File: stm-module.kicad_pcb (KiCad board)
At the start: 2 copper layers, 4 parts, among them U1 STM32G474RETx, U2 TPS7A20xxxDBV

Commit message: add crystal
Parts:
- added C10: 15pF, Capacitor_THT:C_Disc_D5.0mm_W2.5mm_P5.00mm, F.Cu at (136.5, 85.5)
- added C11: 15pF, Capacitor_THT:C_Disc_D5.0mm_W2.5mm_P5.00mm, F.Cu at (136.5, 89.6)
- added C3: 100nF, Capacitor_SMD:C_0805_2012Metric, F.Cu at (122.7, 105.5)
- added C4: 100nF, Capacitor_SMD:C_0805_2012Metric, F.Cu at (127.2, 99.5)
- added C5: 100nF, Capacitor_SMD:C_0805_2012Metric, F.Cu at (127.2, 102.5)
- added C6: 100nF, Capacitor_SMD:C_0805_2012Metric, F.Cu at (127.2, 105.5)
- added C7: 100nF, Capacitor_SMD:C_0805_2012Metric, F.Cu at (131.6, 99.5)
- added C8: 100nF, Capacitor_SMD:C_0805_2012Metric, F.Cu at (131.6, 102.5)
- added C9: 1uF, Capacitor_SMD:C_0805_2012Metric, F.Cu at (131.6, 105.5)
- added R1: 10kΩ, Resistor_SMD:R_0805_2012Metric, F.Cu at (145.2, 93.1)
- added R2: 10kΩ, Resistor_SMD:R_0805_2012Metric, F.Cu at (145.2, 96.0)
- added SW1: Reset, Button_Switch_THT:SW_PUSH_6mm, F.Cu at (135.9, 100.0)
- added Y1: Crystal, Crystal:Crystal_SMD_0603-2Pin_6.0x3.5mm, F.Cu at (139.0, 94.4)
- C1, C2: value 1uf -> 1uF
- moved U2 47.0 mm to (136.4, 108.9)
- moved U1 45.5 mm to (127.7, 90.7)
- moved C2 40.7 mm to (122.7, 102.5)
- moved C1 40.7 mm to (122.7, 99.5)
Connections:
- U1 pad 1: unconnected-(U1-VBAT-Pad1) -> /3.3V
- U1 pad 15: Net-(U1-VSS-Pad15) -> /GND
- U1 pad 27: unconnected-(U1-VSSA-Pad27) -> /GND
- U1 pad 28: unconnected-(U1-VREF+-Pad28) -> /3.3V
- U1 pad 31: Net-(U1-VSS-Pad15) -> /GND
- U1 pad 47: Net-(U1-VSS-Pad15) -> /GND
- U1 pad 5: unconnected-(U1-PF0-Pad5) -> Net-(U1-PF0)
- U1 pad 6: unconnected-(U1-PF1-Pad6) -> Net-(U1-PF1)
- U1 pad 61: unconnected-(U1-PB8-Pad61) -> Net-(U1-PB8)
- U1 pad 63: Net-(U1-VSS-Pad15) -> /GND
- U1 pad 7: unconnected-(U1-PG10-Pad7) -> Net-(U1-PG10)

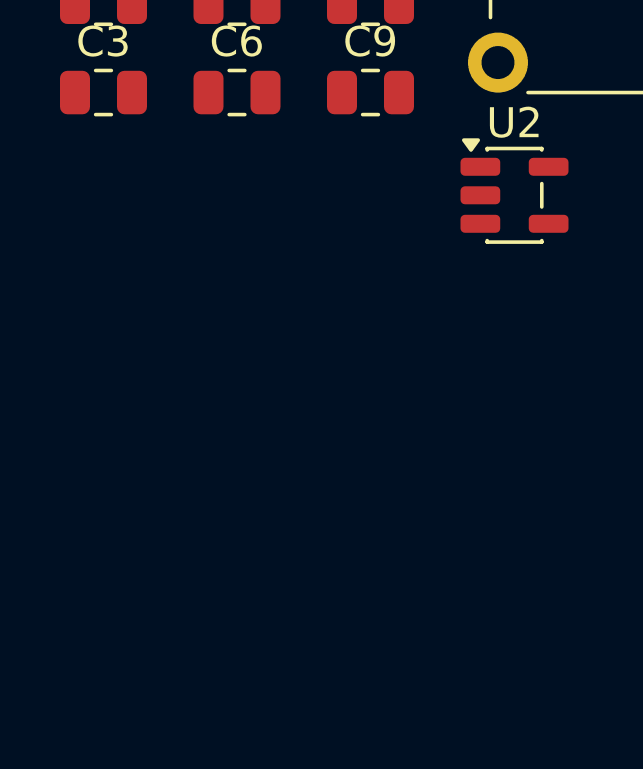
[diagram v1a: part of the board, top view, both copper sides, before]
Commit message: add more caps
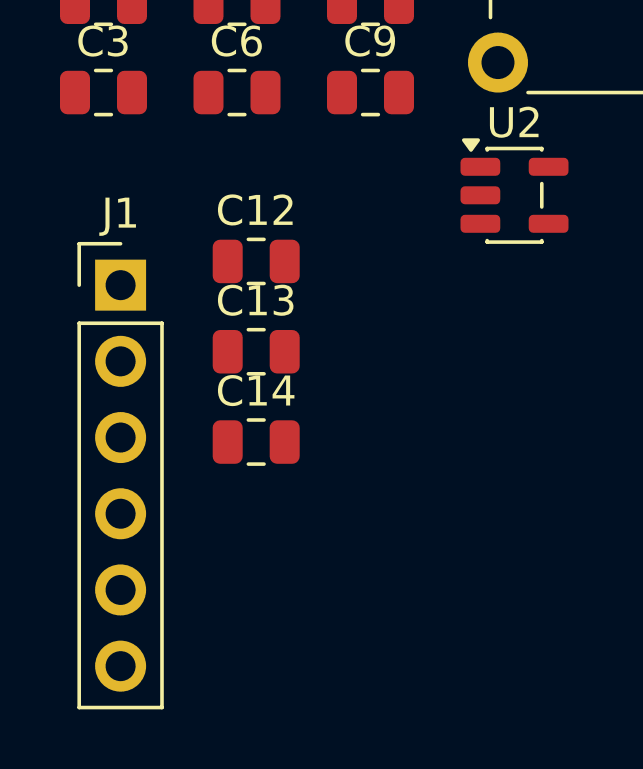
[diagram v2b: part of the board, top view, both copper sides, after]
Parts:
- added C12: 4.7uF, Capacitor_SMD:C_0805_2012Metric, F.Cu at (127.8, 111.1)
- added C13: 100nF, Capacitor_SMD:C_0805_2012Metric, F.Cu at (127.8, 114.1)
- added C14: 1uF, Capacitor_SMD:C_0805_2012Metric, F.Cu at (127.8, 117.1)
- added J1: SWD, Connector_PinHeader_2.54mm:PinHeader_1x06_P2.54mm_Vertical, F.Cu at (123.3, 111.9)
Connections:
- net Net-(U1-PG10) renamed /NRST
- U1 pad 49: unconnected-(U1-PA13-Pad49) -> Net-(J1-Pin_3)
- U1 pad 50: unconnected-(U1-PA14-Pad50) -> Net-(J1-Pin_4)
- U1 pad 56: unconnected-(U1-PB3-Pad56) -> Net-(J1-Pin_6)

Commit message: pcb work
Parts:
- added J2: connectorL, Connector_PinHeader_2.54mm:PinHeader_2x20_P2.54mm_Vertical, B.Cu at (140.5, 85.3)
- added J3: connectorR, Connector_PinHeader_2.54mm:PinHeader_2x20_P2.54mm_Vertical, B.Cu at (185.0, 83.7)
- moved J1 59.1 mm to (166.3, 71.3), turned to -90 degrees
- moved C1 50.6 mm to (169.1, 119.8)
- moved C9 48.5 mm to (177.9, 119.8)
- moved C5 41.8 mm to (168.3, 109.9), turned to -135 degrees
- moved C6 36.7 mm to (163.5, 100.0), turned to -45 degrees
- moved C12 36.7 mm to (163.6, 119.3)
- moved C14 36.7 mm to (163.6, 125.3)
- moved C3 36.1 mm to (154.7, 122.3)
- moved U1 36.1 mm to (159.7, 107.5), turned to 45 degrees
- moved C2 36.1 mm to (154.7, 119.3)
- moved C7 35.8 mm to (159.2, 122.3)
- moved C8 35.8 mm to (159.2, 125.3)
- moved U2 35.5 mm to (165.6, 129.2)
- moved C4 34.4 mm to (157.3, 116.1), turned to 135 degrees
- moved SW1 34.3 mm to (154.5, 128.8)
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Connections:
- net /3.3V renamed +3.3V
- net /5V renamed +5V
- net /GND renamed GND
- net Net-(J1-Pin_3) renamed /PA13
- net Net-(J1-Pin_4) renamed /PA14
- net Net-(J1-Pin_6) renamed /PB3
- net Net-(U1-PB8) renamed /PB8
- U1 pad 10: unconnected-(U1-PC2-Pad10) -> /PC2
- U1 pad 11: unconnected-(U1-PC3-Pad11) -> /PC3
- U1 pad 12: unconnected-(U1-PA0-Pad12) -> /PA0
- U1 pad 13: unconnected-(U1-PA1-Pad13) -> /PA1
- U1 pad 14: unconnected-(U1-PA2-Pad14) -> /PA2
- U1 pad 17: unconnected-(U1-PA3-Pad17) -> /PA3
- U1 pad 18: unconnected-(U1-PA4-Pad18) -> /PA4
- U1 pad 19: unconnected-(U1-PA5-Pad19) -> /PA5
- U1 pad 2: unconnected-(U1-PC13-Pad2) -> /PC13
- U1 pad 20: unconnected-(U1-PA6-Pad20) -> /PA6
- U1 pad 21: unconnected-(U1-PA7-Pad21) -> /PA7
- U1 pad 22: unconnected-(U1-PC4-Pad22) -> /PC4
- U1 pad 23: unconnected-(U1-PC5-Pad23) -> /PC5
- U1 pad 24: unconnected-(U1-PB0-Pad24) -> /PB0
- U1 pad 25: unconnected-(U1-PB1-Pad25) -> /PB1
- U1 pad 26: unconnected-(U1-PB2-Pad26) -> /PB2
- U1 pad 3: unconnected-(U1-PC14-Pad3) -> /PC14
- U1 pad 30: unconnected-(U1-PB10-Pad30) -> /PB10
- U1 pad 33: unconnected-(U1-PB11-Pad33) -> /PB11
- U1 pad 34: unconnected-(U1-PB12-Pad34) -> /PB12
- U1 pad 35: unconnected-(U1-PB13-Pad35) -> /PB13
- U1 pad 36: unconnected-(U1-PB14-Pad36) -> /PB14
- U1 pad 37: unconnected-(U1-PB15-Pad37) -> /PB15
- U1 pad 38: unconnected-(U1-PC6-Pad38) -> /PC6
- U1 pad 39: unconnected-(U1-PC7-Pad39) -> /PC7
- U1 pad 4: unconnected-(U1-PC15-Pad4) -> /PC15
- U1 pad 40: unconnected-(U1-PC8-Pad40) -> /PC8
- U1 pad 41: unconnected-(U1-PC9-Pad41) -> /PC9
- U1 pad 42: unconnected-(U1-PA8-Pad42) -> /PA8
- U1 pad 43: unconnected-(U1-PA9-Pad43) -> /PA9
- U1 pad 44: unconnected-(U1-PA10-Pad44) -> /PA10
- U1 pad 45: unconnected-(U1-PA11-Pad45) -> /PA11
- U1 pad 46: unconnected-(U1-PA12-Pad46) -> /PA12
- U1 pad 51: unconnected-(U1-PA15-Pad51) -> /PA15
- U1 pad 52: unconnected-(U1-PC10-Pad52) -> /PC10
- U1 pad 53: unconnected-(U1-PC11-Pad53) -> /PC11
- U1 pad 54: unconnected-(U1-PC12-Pad54) -> /PC12
- U1 pad 55: unconnected-(U1-PD2-Pad55) -> /PD2
- U1 pad 57: unconnected-(U1-PB4-Pad57) -> /PB4
- U1 pad 58: unconnected-(U1-PB5-Pad58) -> /PB5
- U1 pad 59: unconnected-(U1-PB6-Pad59) -> /PB6
- U1 pad 60: unconnected-(U1-PB7-Pad60) -> /PB7
- U1 pad 62: unconnected-(U1-PB9-Pad62) -> /PB9
- U1 pad 8: unconnected-(U1-PC0-Pad8) -> /PC0
- U1 pad 9: unconnected-(U1-PC1-Pad9) -> /PC1
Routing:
- net +3.3V: track 0.00 -> 7.98 mm
- added copper zone on F.Cu, net GND
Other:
- board outline added: 86.3 x 83.5 mm

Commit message: updates
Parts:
- moved SW1 57.6 mm to (182.2, 78.2)
- moved C3 33.0 mm to (186.2, 132.0), turned to -135 degrees
- moved C7 32.7 mm to (173.4, 92.8), turned to 45 degrees
- moved C2 31.7 mm to (176.2, 142.5), turned to 90 degrees
- moved Y1 29.2 mm to (169.9, 139.2)
- moved C4 27.8 mm to (176.2, 136.5)
- moved J2 27.4 mm to (162.4, 101.8)
- moved C10 27.1 mm to (171.0, 79.9)
- moved C8 25.7 mm to (184.4, 130.1), turned to -45 degrees
- moved C14 25.4 mm to (187.7, 133.4), turned to -135 degrees
- moved U1 25.0 mm to (176.4, 126.0)
- moved C13 22.9 mm to (167.2, 125.8)
- moved C5 22.9 mm to (185.4, 125.1), turned to 45 degrees
- moved C11 22.4 mm to (179.9, 96.1)
- moved U2 21.4 mm to (180.1, 144.9)
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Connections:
- J3 pad 1: unconnected-(J3-Pin_1-Pad1) -> GND
- J3 pad 10: unconnected-(J3-Pin_10-Pad10) -> /PC7
- J3 pad 11: unconnected-(J3-Pin_11-Pad11) -> /PB14
- J3 pad 12: unconnected-(J3-Pin_12-Pad12) -> /PB15
- J3 pad 13: unconnected-(J3-Pin_13-Pad13) -> /PB12
- J3 pad 14: unconnected-(J3-Pin_14-Pad14) -> /PB13
- J3 pad 15: unconnected-(J3-Pin_15-Pad15) -> +3.3V
- J3 pad 16: unconnected-(J3-Pin_16-Pad16) -> /PB11
- J3 pad 17: unconnected-(J3-Pin_17-Pad17) -> GND
- J3 pad 18: unconnected-(J3-Pin_18-Pad18) -> GND
- J3 pad 19: unconnected-(J3-Pin_19-Pad19) -> GND
- J3 pad 2: unconnected-(J3-Pin_2-Pad2) -> /PA12
- J3 pad 20: unconnected-(J3-Pin_20-Pad20) -> GND
- J3 pad 21: unconnected-(J3-Pin_21-Pad21) -> GND
- J3 pad 22: unconnected-(J3-Pin_22-Pad22) -> GND
- J3 pad 23: unconnected-(J3-Pin_23-Pad23) -> GND
- J3 pad 24: unconnected-(J3-Pin_24-Pad24) -> GND
- J3 pad 25: unconnected-(J3-Pin_25-Pad25) -> GND
- J3 pad 26: unconnected-(J3-Pin_26-Pad26) -> GND
- J3 pad 27: unconnected-(J3-Pin_27-Pad27) -> GND
- J3 pad 28: unconnected-(J3-Pin_28-Pad28) -> GND
- J3 pad 29: unconnected-(J3-Pin_29-Pad29) -> /PB10
- J3 pad 3: unconnected-(J3-Pin_3-Pad3) -> /PA10
- J3 pad 30: unconnected-(J3-Pin_30-Pad30) -> +3.3V
- J3 pad 31: unconnected-(J3-Pin_31-Pad31) -> /PB2
- J3 pad 32: unconnected-(J3-Pin_32-Pad32) -> /PB1
- J3 pad 33: unconnected-(J3-Pin_33-Pad33) -> /PB0
- J3 pad 34: unconnected-(J3-Pin_34-Pad34) -> /PC5
- J3 pad 35: unconnected-(J3-Pin_35-Pad35) -> /PC4
- J3 pad 36: unconnected-(J3-Pin_36-Pad36) -> /PA7
- J3 pad 37: unconnected-(J3-Pin_37-Pad37) -> /PA6
- J3 pad 38: unconnected-(J3-Pin_38-Pad38) -> /PA5
- J3 pad 39: unconnected-(J3-Pin_39-Pad39) -> /PA4
- J3 pad 4: unconnected-(J3-Pin_4-Pad4) -> /PA11
- J3 pad 40: unconnected-(J3-Pin_40-Pad40) -> /PA3
- J3 pad 5: unconnected-(J3-Pin_5-Pad5) -> /PA8
- J3 pad 6: unconnected-(J3-Pin_6-Pad6) -> /PA9
- J3 pad 7: unconnected-(J3-Pin_7-Pad7) -> /PC8
- J3 pad 8: unconnected-(J3-Pin_8-Pad8) -> /PC9
- J3 pad 9: unconnected-(J3-Pin_9-Pad9) -> /PC6
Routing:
- net GND: track 0.00 -> 44.0 mm
- net /PA4: track 0.00 -> 24.9 mm
- net /PA12: track 0.00 -> 23.2 mm
- net /PA10: track 0.00 -> 23.2 mm
- net /PA6: track 0.00 -> 22.8 mm
- net /PA3: track 0.00 -> 22.6 mm
- net /PA8: track 0.00 -> 21.0 mm
- net /PA11: track 0.00 -> 20.9 mm
- net /PC4: track 0.00 -> 20.6 mm
- net /PA5: track 0.00 -> 20.5 mm
- net /PC8: track 0.00 -> 18.9 mm
- net /PA9: track 0.00 -> 18.7 mm
- net /PB0: track 0.00 -> 18.5 mm
- net /PA7: track 0.00 -> 18.4 mm
- net /PC6: track 0.00 -> 16.8 mm
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- added copper zone on B.Cu, net GND

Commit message: pcb updates
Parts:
- added C15: 10uF, Capacitor_SMD:C_0805_2012Metric, F.Cu at (178.3, 147.8)
- added J4: power, Connector_PinHeader_2.54mm:PinHeader_1x04_P2.54mm_Vertical, F.Cu at (174.1, 150.7)
- C12: value 4.7uF -> 10uF
- C13, C3, C4, C5, C6, C7, C8: footprint Capacitor_SMD:C_0805_2012Metric -> Capacitor_SMD:C_0603_1608Metric
- moved C11 46.2 mm to (165.3, 140.0), turned to 45 degrees
- moved C12 45.8 mm to (186.1, 151.1), turned to 180 degrees
- moved C10 41.1 mm to (164.6, 120.5), turned to -90 degrees
- moved C1 39.6 mm to (185.6, 148.2), turned to -90 degrees
- moved SW1 30.2 mm to (175.4, 107.7), turned to -45 degrees
- moved C7 29.9 mm to (167.9, 122.2), turned to -90 degrees
- moved C3 19.4 mm to (168.0, 125.3), turned to -90 degrees
- moved C13 17.1 mm to (183.6, 130.6)
- moved C6 15.3 mm to (179.4, 117.3), turned to -135 degrees
- moved R1 15.0 mm to (181.7, 114.7), turned to 45 degrees
- moved Y1 8.84 mm to (167.7, 130.6), turned to 135 degrees
- moved C2 3.83 mm to (178.3, 145.7), turned to 180 degrees
- moved U2 3.18 mm to (182.4, 147.1)
- moved C14 2.86 mm to (186.4, 130.9), turned to 135 degrees
- moved C9 2.53 mm to (187.4, 126.6), turned to 45 degrees
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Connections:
- C13 pad 1: +3.3V -> GND
- C13 pad 2: GND -> +3.3V
- C2 pad 2: +5V -> GND
- C4 pad 1: +3.3V -> GND
- C4 pad 2: GND -> +3.3V
- C5 pad 1: +3.3V -> GND
- C5 pad 2: GND -> +3.3V
- C6 pad 1: +3.3V -> GND
- C6 pad 2: GND -> +3.3V
- C7 pad 1: +3.3V -> GND
- C7 pad 2: GND -> +3.3V
- C8 pad 1: +3.3V -> GND
- C8 pad 2: GND -> +3.3V
- J2 pad 10: unconnected-(J2-Pin_10-Pad10) -> /PB4
- J2 pad 11: unconnected-(J2-Pin_11-Pad11) -> /PB5
- J2 pad 12: unconnected-(J2-Pin_12-Pad12) -> /PB6
- J2 pad 13: unconnected-(J2-Pin_13-Pad13) -> /PB7
- J2 pad 14: unconnected-(J2-Pin_14-Pad14) -> /PB8
- J2 pad 15: unconnected-(J2-Pin_15-Pad15) -> /PB9
- J2 pad 16: unconnected-(J2-Pin_16-Pad16) -> +3.3V
- J2 pad 17: unconnected-(J2-Pin_17-Pad17) -> /PC13
- J2 pad 18: unconnected-(J2-Pin_18-Pad18) -> /PC14
- J2 pad 19: unconnected-(J2-Pin_19-Pad19) -> /PC15
- J2 pad 2: unconnected-(J2-Pin_2-Pad2) -> /PA13
- J2 pad 21: unconnected-(J2-Pin_21-Pad21) -> GND
- J2 pad 22: unconnected-(J2-Pin_22-Pad22) -> GND
- J2 pad 23: unconnected-(J2-Pin_23-Pad23) -> GND
- J2 pad 24: unconnected-(J2-Pin_24-Pad24) -> GND
- J2 pad 25: unconnected-(J2-Pin_25-Pad25) -> GND
- J2 pad 26: unconnected-(J2-Pin_26-Pad26) -> GND
- J2 pad 27: unconnected-(J2-Pin_27-Pad27) -> GND
- J2 pad 28: unconnected-(J2-Pin_28-Pad28) -> GND
- J2 pad 29: unconnected-(J2-Pin_29-Pad29) -> GND
- J2 pad 3: unconnected-(J2-Pin_3-Pad3) -> /PA14
- J2 pad 30: unconnected-(J2-Pin_30-Pad30) -> GND
- J2 pad 31: unconnected-(J2-Pin_31-Pad31) -> GND
- J2 pad 32: unconnected-(J2-Pin_32-Pad32) -> GND
- J2 pad 33: unconnected-(J2-Pin_33-Pad33) -> /PC0
- J2 pad 34: unconnected-(J2-Pin_34-Pad34) -> GND
- J2 pad 35: unconnected-(J2-Pin_35-Pad35) -> /PC2
- J2 pad 36: unconnected-(J2-Pin_36-Pad36) -> /PC1
- J2 pad 37: unconnected-(J2-Pin_37-Pad37) -> /PA0
- J2 pad 38: unconnected-(J2-Pin_38-Pad38) -> /PC3
- J2 pad 39: unconnected-(J2-Pin_39-Pad39) -> /PA2
- J2 pad 4: unconnected-(J2-Pin_4-Pad4) -> /PA15
- J2 pad 40: unconnected-(J2-Pin_40-Pad40) -> /PA1
- J2 pad 5: unconnected-(J2-Pin_5-Pad5) -> /PC10
- J2 pad 6: unconnected-(J2-Pin_6-Pad6) -> /PC11
- J2 pad 7: unconnected-(J2-Pin_7-Pad7) -> /PC12
- J2 pad 8: unconnected-(J2-Pin_8-Pad8) -> /PD2
- J2 pad 9: unconnected-(J2-Pin_9-Pad9) -> /PB3
- J3 pad 15: +3.3V -> /PB10
- J3 pad 17: GND -> +3.3V
- J3 pad 29: /PB10 -> GND
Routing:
- net +3.3V: track 21.5 -> 251.1 mm
- net GND: track 44.0 -> 17.0 mm, vias 0 -> 6
- net /PA1: track 0.00 -> 25.3 mm
- net /PA13: track 0.00 -> 25.0 mm
- net /PC3: track 0.00 -> 23.9 mm
- net /PA2: track 0.00 -> 23.1 mm
- net /NRST: track 0.00 -> 23.0 mm
- net /PA15: track 0.00 -> 22.9 mm
- net /PC1: track 0.00 -> 22.5 mm
- net /PA0: track 0.00 -> 21.5 mm
- net /PC11: track 0.00 -> 20.7 mm
- net /PA14: track 0.00 -> 20.6 mm
- net /PC2: track 0.00 -> 20.1 mm
- net /PD2: track 0.00 -> 19.2 mm
- net /PC0: track 0.00 -> 18.8 mm
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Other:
- board size 86.3 x 83.5 mm -> 39.3 x 83.5 mm

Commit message: finish main routing
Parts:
- J1: value SWD -> Conn_01x05_Pin; footprint Connector_PinHeader_2.54mm:PinHeader_1x06_P2.54mm_Vertical -> Connector_PinHeader_2.54mm:PinHeader_1x05_P2.54mm_Vertical
- moved J1 32.5 mm to (170.3, 103.6), turned to 90 degrees
- moved R2 27.3 mm to (165.3, 117.7), turned to -90 degrees
- moved C4 0.10 mm to (175.2, 135.2)
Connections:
- J1 pad 1: +3.3V -> /NRST
- J1 pad 2: GND -> /PA13
- J1 pad 3: /PA13 -> /PA14
- J1 pad 4: /PA14 -> GND
- J1 pad 5: /NRST -> +3.3V
- J3 pad 30: +3.3V -> GND
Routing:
- net /PA14: track 20.6 -> 45.6 mm
- net /PA13: track 25.0 -> 39.7 mm
- net /NRST: track 23.0 -> 37.6 mm
- net GND: track 17.0 -> 21.4 mm
- net +3.3V: track 251.1 -> 248.2 mm
- net /PB7: track 12.7 -> 14.1 mm
- net /PB8: track 15.1 -> 16.4 mm
- net /PB9: track 12.0 -> 12.8 mm
- net /PB6: track 16.4 -> 17.2 mm
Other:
- board size 39.3 x 83.5 mm -> 39.3 x 56.1 mm

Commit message: more pcb updates
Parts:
- added D1: PWR LED, LED_SMD:LED_0805_2012Metric, F.Cu at (176.0, 141.1)
- added D2: RUN LED, LED_SMD:LED_0805_2012Metric, F.Cu at (178.1, 141.1)
- added D3: CAN LED, LED_SMD:LED_0805_2012Metric, F.Cu at (180.2, 141.1)
- added D4: FAULT LED, LED_SMD:LED_0805_2012Metric, F.Cu at (182.3, 141.1)
- added J5: USB_C_Receptacle_USB2.0_16P, Connector_USB:USB_C_Receptacle_HRO_TYPE-C-31-M-12, F.Cu at (182.9, 101.2)
- added R3: 330Ω, Resistor_SMD:R_0805_2012Metric, F.Cu at (173.9, 141.8)
- added R4: 220Ω, Resistor_SMD:R_0805_2012Metric, F.Cu at (178.1, 137.7)
- added R5: 1kΩ, Resistor_SMD:R_0805_2012Metric, F.Cu at (180.2, 137.7)
- added R6: 1kΩ, Resistor_SMD:R_0805_2012Metric, F.Cu at (182.3, 137.7)
- added R7: 5.1kΩ, Resistor_SMD:R_0805_2012Metric, F.Cu at (185.6, 107.4)
- added R8: 5.1kΩ, Resistor_SMD:R_0805_2012Metric, F.Cu at (180.8, 107.4)
- added REF**: MountingHole_3.2mm_M3, MountingHole:MountingHole_3.2mm_M3, F.Cu at (196.8, 99.3)
- added REF**: MountingHole_3.2mm_M3, MountingHole:MountingHole_3.2mm_M3, F.Cu at (196.7, 153.8)
- added REF**: MountingHole_3.2mm_M3, MountingHole:MountingHole_3.2mm_M3, F.Cu at (156.3, 99.2)
- added REF**: MountingHole_3.2mm_M3, MountingHole:MountingHole_3.2mm_M3, F.Cu at (156.2, 153.7)
- moved SW1 7.84 mm to (176.7, 115.5), turned to 135 degrees
- moved J1 5.39 mm to (165.4, 101.3)
- moved R1 0.32 mm to (181.4, 114.6)
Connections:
- J2 pad 20: unconnected-(J2-Pin_20-Pad20) -> GND
- J3 pad 2: /PA12 -> unconnected-(J3-Pin_2-Pad2)
- J3 pad 4: /PA11 -> unconnected-(J3-Pin_4-Pad4)
- U1 pad 45: /PA11 -> /D-
- U1 pad 46: /PA12 -> /D+
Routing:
- net +3.3V: track 248.2 -> 299.9 mm
- net /PA12: track 23.2 -> 0.00 mm
- net /PA11: track 20.9 -> 0.00 mm
- net /D-: track 0.00 -> 20.0 mm
- net /D+: track 0.00 -> 19.6 mm
- net /NRST: track 37.6 -> 46.5 mm
- net Net-(J5-VBUS-PadA4): track 0.00 -> 6.99 mm
- net /PA14: track 45.6 -> 39.7 mm
- net /PA13: track 39.7 -> 34.3 mm
- net Net-(D1-A): track 0.00 -> 2.40 mm
- net Net-(J5-SBU1): track 0.00 -> 2.21 mm
- net Net-(J5-SBU2): track 0.00 -> 2.21 mm
- net /PA3: track 22.6 -> 24.6 mm
- net Net-(D4-A): track 0.00 -> 1.55 mm
- net Net-(D3-A): track 0.00 -> 1.55 mm
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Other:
- board size 39.3 x 56.1 mm -> 45.2 x 59.1 mm

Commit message: final changes
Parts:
- removed the REF** at (196.8, 99.3)
- removed the REF** at (196.7, 153.8)
- removed the REF** at (156.3, 99.2)
- removed the REF** at (156.2, 153.7)
- added REF**: MountingHole_3.2mm_M3, MountingHole:MountingHole_3.2mm_M3, F.Cu at (196.8, 99.3)
- added REF**: MountingHole_3.2mm_M3, MountingHole:MountingHole_3.2mm_M3, F.Cu at (196.9, 153.7)
- added REF**: MountingHole_3.2mm_M3, MountingHole:MountingHole_3.2mm_M3, F.Cu at (156.2, 153.8)
- added REF**: MountingHole_3.2mm_M3, MountingHole:MountingHole_3.2mm_M3, F.Cu at (156.2, 99.3)
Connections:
- J3 pad 17: +3.3V -> GND
- J3 pad 2: unconnected-(J3-Pin_2-Pad2) -> /D+
- J3 pad 4: unconnected-(J3-Pin_4-Pad4) -> /D-
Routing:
- net /D+: track 19.6 -> 27.6 mm
- net /D-: track 20.0 -> 27.3 mm
- net Net-(J5-VBUS-PadA4): track 6.99 -> 0.00 mm
- net +3.3V: track 299.9 -> 299.0 mm
- net /NRST: track 46.5 -> 45.9 mm
